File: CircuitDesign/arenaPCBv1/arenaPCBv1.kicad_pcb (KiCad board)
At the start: 2 copper layers, 105.4 x 63.5 mm, 28 parts, among them Q1 IRLB3034

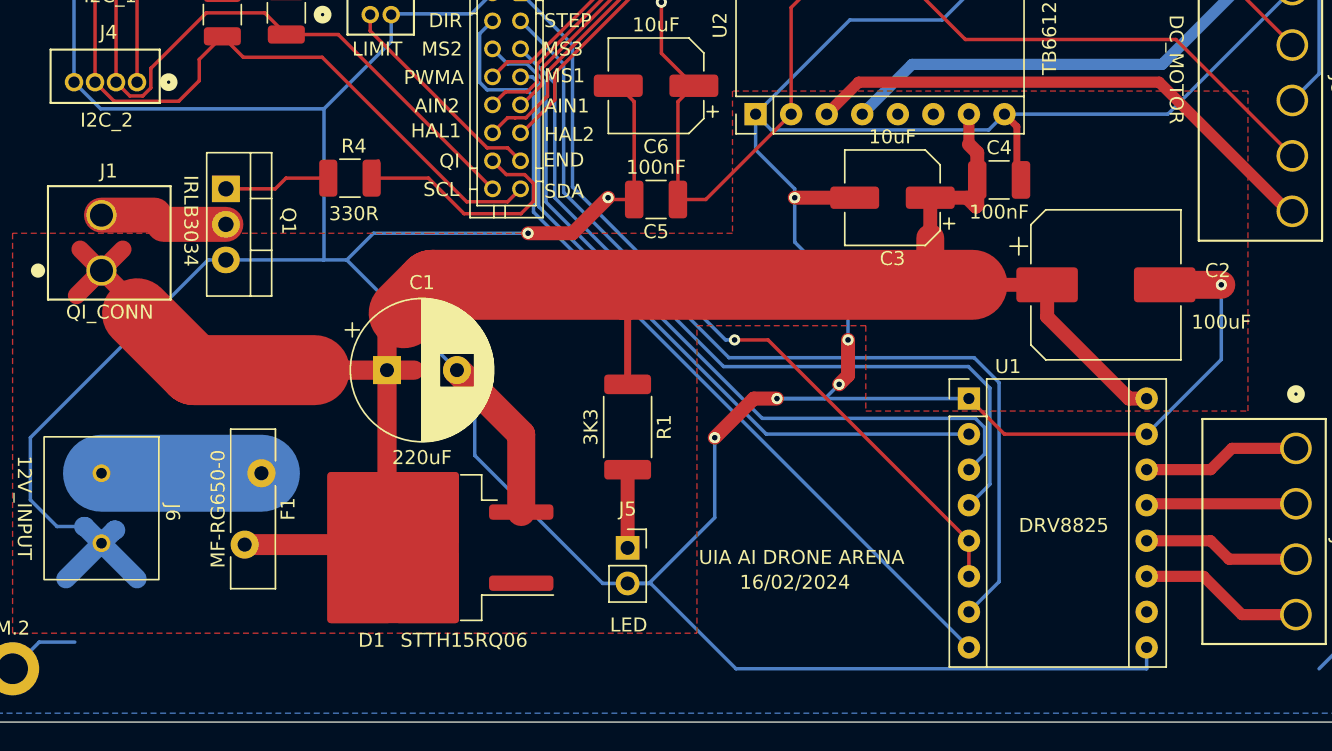
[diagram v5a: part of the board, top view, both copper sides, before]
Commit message: pcb finished v2
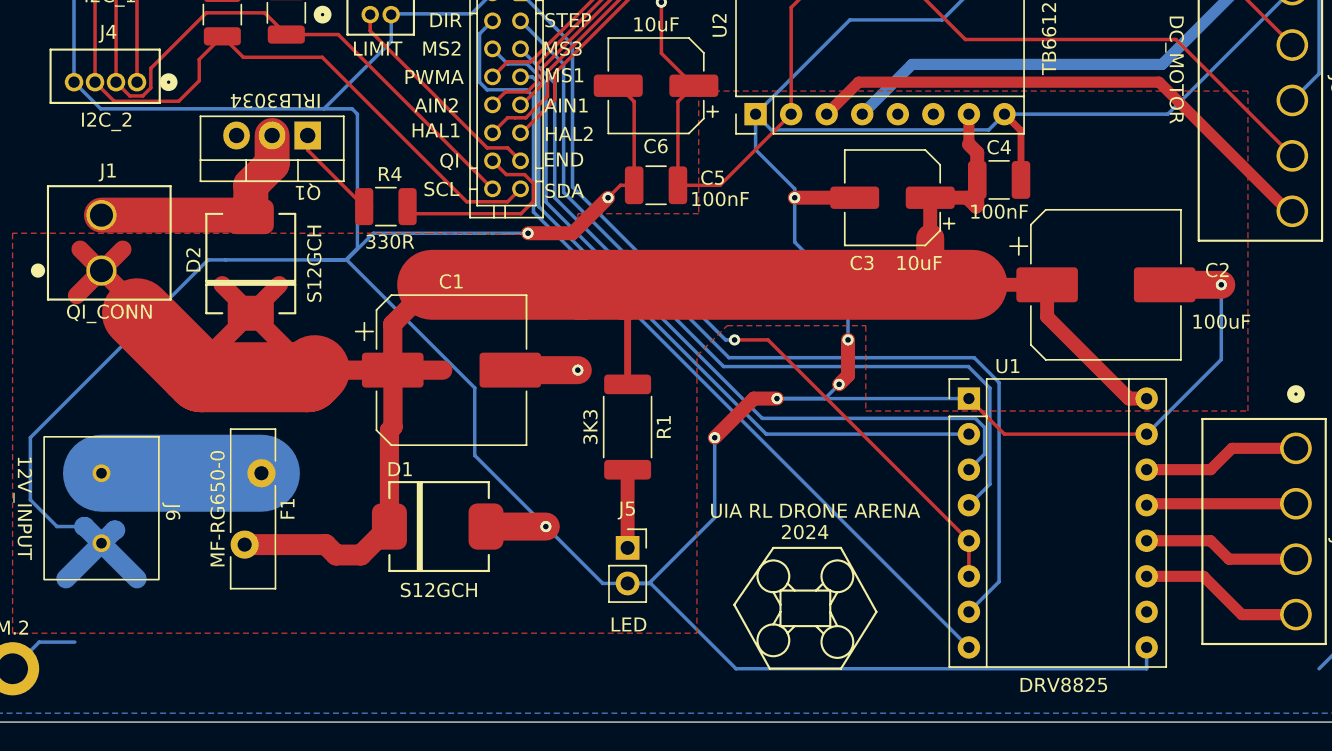
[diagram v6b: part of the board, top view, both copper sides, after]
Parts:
- added D2: S12GCH, 2_Bachelors_footprints:S12GCH, F.Cu at (119.9, 80.5)
- C1: footprint Capacitor_THT:CP_Radial_D10.0mm_P5.00mm -> Capacitor_SMD:CP_Elec_10x10.5
- D1: value STTH15RQ06 -> S12GCH; footprint Package_TO_SOT_SMD:TO-263-2 -> 2_Bachelors_footprints:S12GCH
- moved Q1 7.16 mm to (121.4, 71.1), turned to 180 degrees
- moved C1 4.61 mm to (134.2, 87.9)
- moved R4 3.27 mm to (129.5, 76.2)
- moved D1 2.15 mm to (133.1, 99.1), turned to 0 degrees
- moved C5 1.02 mm to (148.8, 74.7)
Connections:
- D1 pad 1: (no net) -> +12V
- D1 pad 2: +12V -> GND
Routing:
- net +12V: track 144.2 -> 166.5 mm
- net /D: track 10.1 -> 17.8 mm
- net Net-(J9-QI): track 18.9 -> 14.4 mm
- net +3.3V: track 183.8 -> 182.4 mm
- net GND: track 408.6 -> 409.1 mm, vias 8 -> 10
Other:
- board text added: "2024"
- board text added: "UIA RL DRONE ARENA"
- board text removed: "16/02/2024"
- board text removed: "UIA AI DRONE ARENA"

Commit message: pcb updates and other stuff
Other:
- board text added: "VCC"
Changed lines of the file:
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@@
+    (effects (font (size 1 1) (thickness 0.15)) (justify left bottom))
+  )
+  (gr_text "VCC" (at 148.59 101.346) (layer "F.SilkS")
     (effects (font (size 1 1) (thickness 0.15)) (justify left bottom))
   )
@@
     (effects (font (size 1 1) (thickness 0.15)) (justify left bottom))
   )
+  (gr_text "GND" (at 148.59 103.886) (layer "F.SilkS")
+    (effects (font (size 1 1) (thickness 0.15)) (justify left bottom))
+  )

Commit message: SMD PCB done
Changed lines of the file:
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@@
   (gr_line (start 154.432 104.648) (end 157.226 100.584)
     (stroke (width 0.15) (type default)) (layer "F.SilkS"))
-  (gr_rect (start 157.734 106.172) (end 161.29 103.632)
+  (gr_rect (start 157.734 103.632) (end 161.29 106.172)
     (stroke (width 0.15) (type default)) (fill none) (layer "F.SilkS"))
   (gr_line (start 161.29 104.648) (end 161.798 103.751922)
@@
         (xy 143.256 78.232)
         (xy 132.715 78.105)
-        (xy 132.715 78.105)
         (xy 102.87 78.105)
